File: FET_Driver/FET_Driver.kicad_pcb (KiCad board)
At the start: 2 copper layers, 32 x 20 mm, 8 parts, among them J101 Interface, J102 Out, Q101 IRF5210SPbF, U101 EL3H7(C)(TA)-G

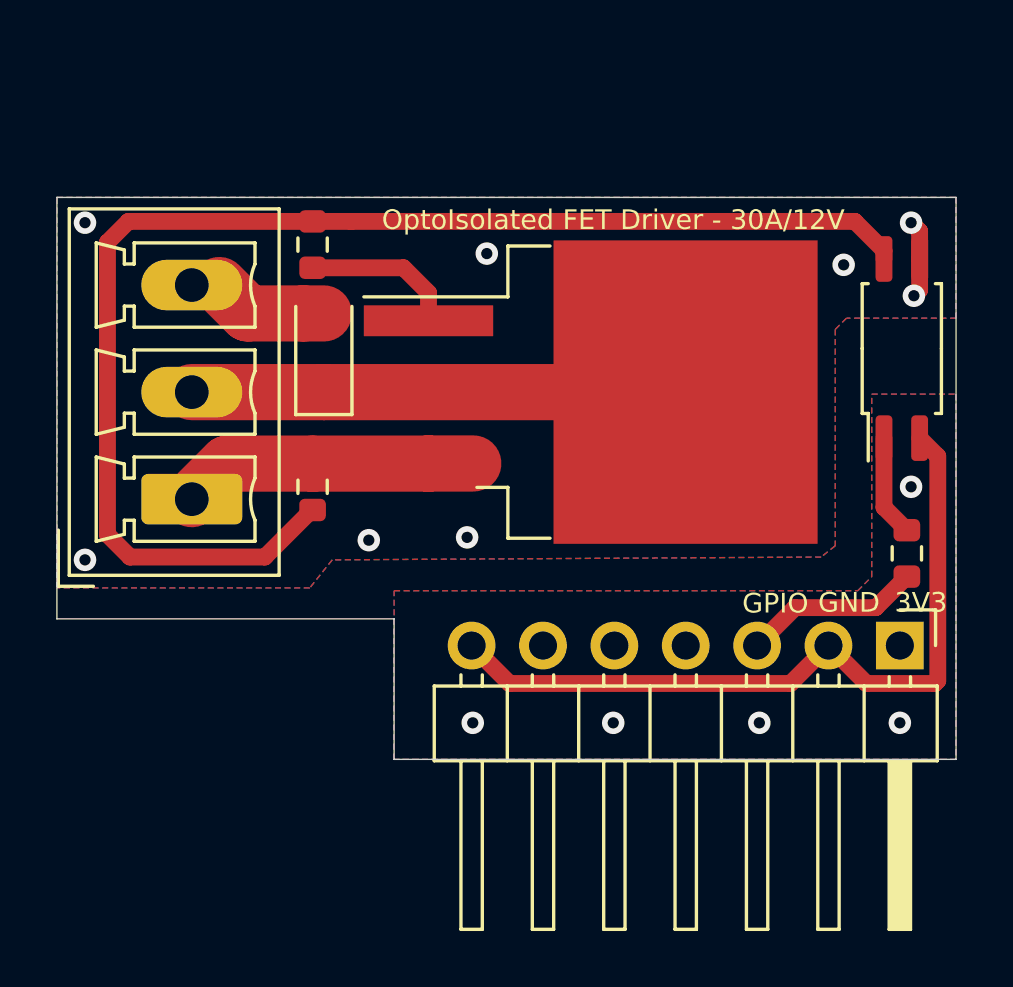
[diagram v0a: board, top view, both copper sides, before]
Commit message: Re-arrange FET Driver  PCB  for better High current tracks
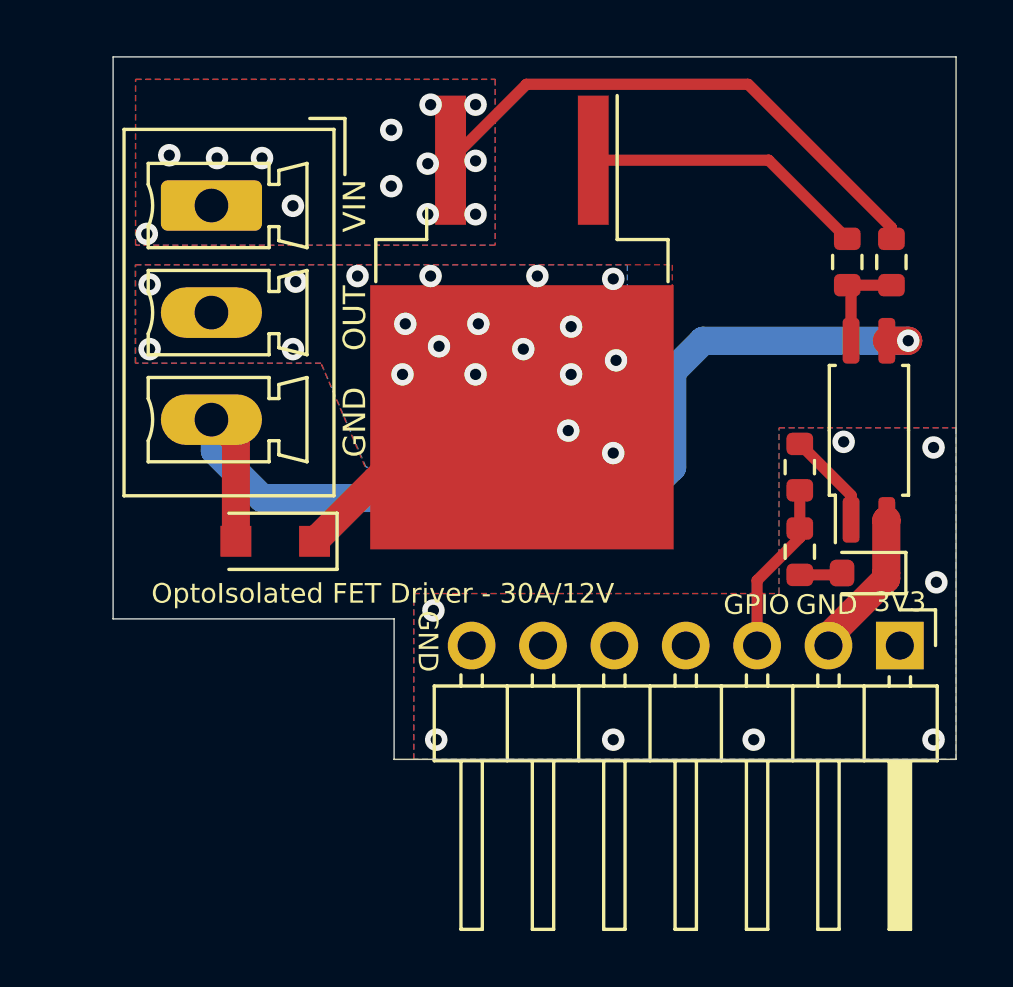
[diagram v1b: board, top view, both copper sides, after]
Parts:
- added D102: GREEN LED, LED_SMD:LED_0603_1608Metric, F.Cu at (136.7, 86.4)
- added R103: 1k, Resistor_SMD:R_0603_1608Metric, F.Cu at (134.4, 85.6)
- Q101: value IRF5210SPbF -> IRF5210STRLPBF
- moved R101 22.1 mm to (137.7, 75.3)
- moved R102 19.0 mm to (136.1, 75.3), turned to 270 degrees
- moved J102 10.5 mm to (113.5, 73.3), turned to 270 degrees
- moved D101 6.93 mm to (115.8, 85.2), turned to 180 degrees
- moved R901 4.89 mm to (134.4, 82.6)
- moved Q101 3.49 mm to (124.5, 77.5), turned to 270 degrees
- moved U101 3.14 mm to (136.9, 81.3)
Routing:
- net Net-(R101-Pad2): track 47.4 -> 3.60 mm
- net /ISO_GND: track 6.95 -> 36.2 mm, vias 8 -> 1
- net GND: track 27.2 -> 5.33 mm, vias 5 -> 8
- net /ISO_OUT: track 17.6 -> 6.24 mm, vias 0 -> 19
- net /ISO_VIN: track 10.5 -> 19.3 mm, vias 0 -> 13
- net Net-(Q101-Pad1): track 5.49 -> 10.2 mm
- net Net-(D102-Pad2): track 0.00 -> 1.53 mm
- added copper zone on B.Cu, net /ISO_OUT
- added copper zone on F.Cu, net /ISO_OUT
- added copper zone on B.Cu, net /ISO_VIN
- added copper zone on F.Cu, net /ISO_VIN
- removed copper zone on B.Cu, net /ISO_GND
- removed copper zone on F.Cu, net /ISO_GND
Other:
- board size 32 x 20 mm -> 30 x 25 mm
- board text added: "OUT"
- board text added: "VIN"
- board text removed: "GND ISO"
- board text removed: "Hole here is for Single pin to support board edge if needed for connectors when Horizontal on SH-ESP32"
- board text removed: "OUT ISO"
- board text removed: "VIN ISO"

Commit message: Change FET VIN/OUT connector to 4 Pin to reduce stock parts
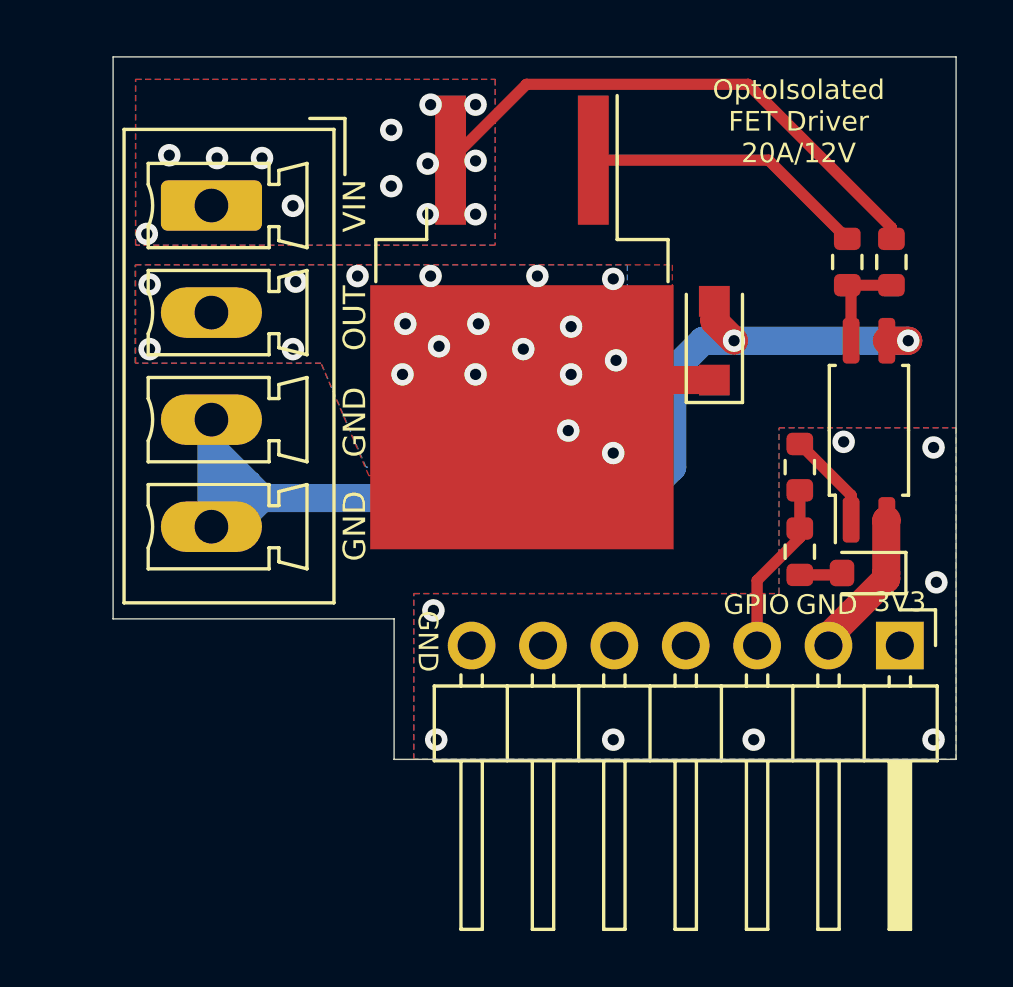
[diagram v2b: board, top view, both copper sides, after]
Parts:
- J102: footprint Connector_Phoenix_MC:PhoenixContact_MCV_1,5_3-G-3.81_1x03_P3.81mm_Vertical -> Connector_Phoenix_MC:PhoenixContact_MCV_1,5_4-G-3.81_1x04_P3.81mm_Vertical
- moved D101 17.2 mm to (131.4, 78.1), turned to 90 degrees
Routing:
- net /ISO_GND: track 36.2 -> 43.2 mm, vias 1 -> 2
- net /ISO_OUT: track 6.24 -> 5.18 mm
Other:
- board text added: "OptoIsolated FET Driver 20A/12V"
- board text removed: "OptoIsolated FET Driver - 30A/12V"
